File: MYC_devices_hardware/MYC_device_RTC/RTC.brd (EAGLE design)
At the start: 64.8 x 54.9 mm, 30 parts, among them IC1 MEGA8-P, IC2 7805T, Q1 20MHz, X1 8-15V, X2 1503_09, X3 1503_09

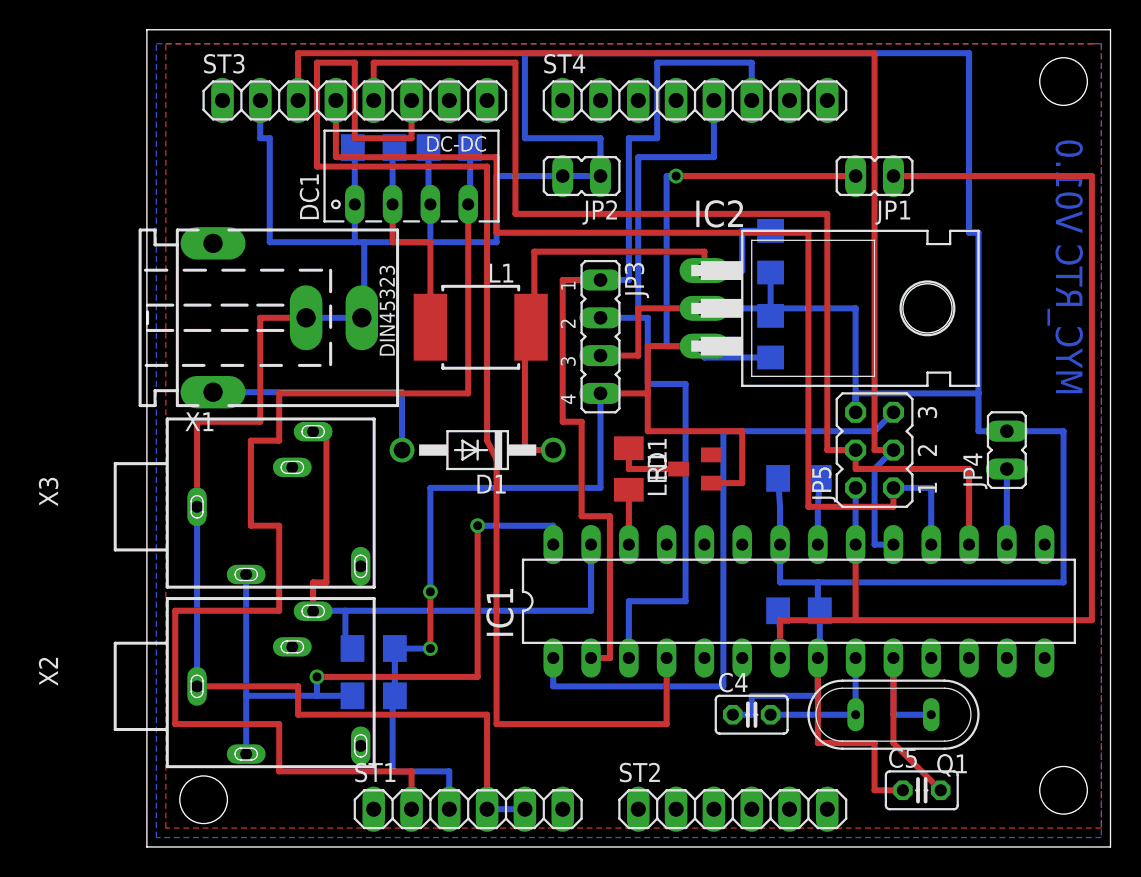
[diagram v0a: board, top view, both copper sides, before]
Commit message: some changes of DTMF devices
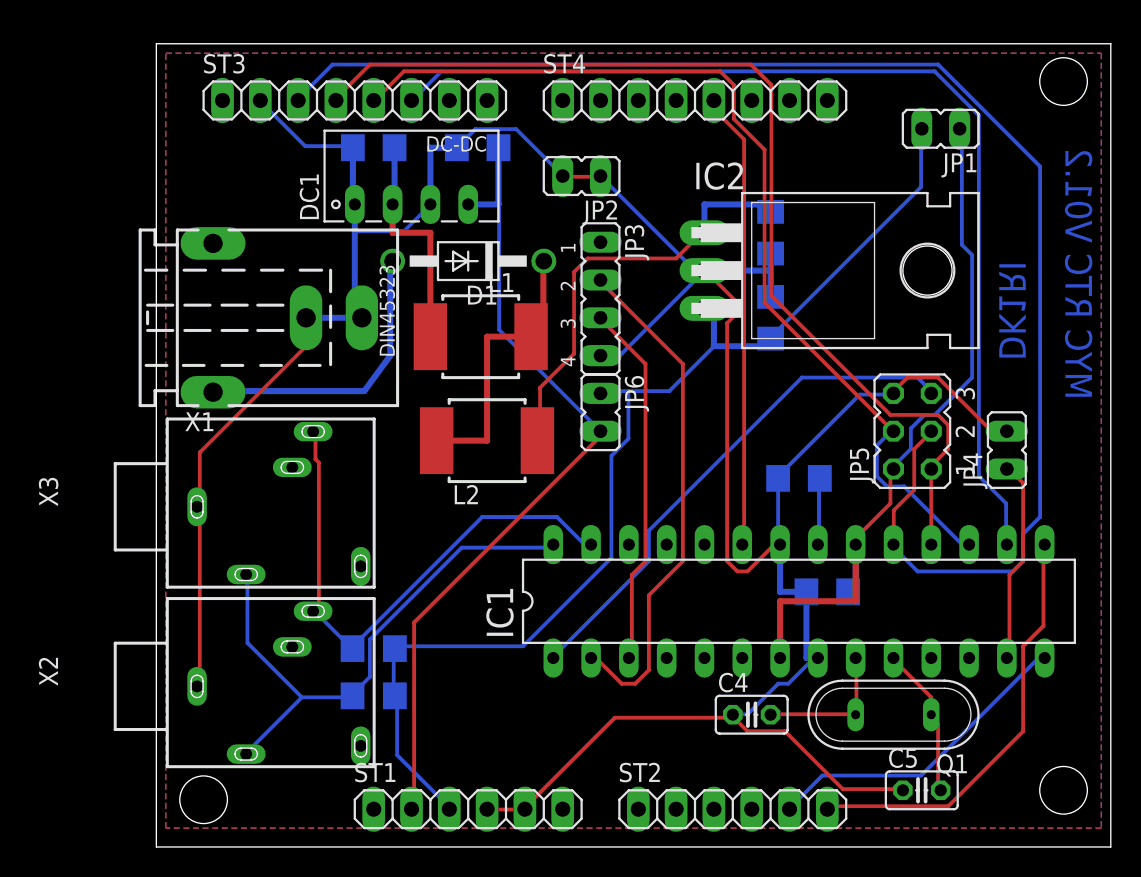
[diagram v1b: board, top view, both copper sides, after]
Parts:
- removed LED1: PL006-WCY01, led:SOT23
- removed R1: 4k7, resistor:M1206
- added JP6: USB2, jumper:JP1
- added L2: 100u, inductor-neosid:MS85
- moved D1 12.7 mm to (20.3, 39.4)
- moved JP1 5.46 mm to (52.1, 48.3)
- moved JP5 2.84 mm to (50.2, 27.9)
- moved IC2 2.54 mm to (46.4, 38.7)
- moved JP3 2.54 mm to (29.2, 36.8)
- moved C6 2.29 mm to (44.5, 17.1), turned to 0 degrees
- moved C7 1.90 mm to (21.0, 47.0)
- moved C2 1.27 mm to (40.6, 35.6)
- moved C1 1.27 mm to (40.6, 41.3)
- moved L1 0.63 mm to (21.2, 34.3)
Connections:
- removed net N$12: IC1.3, JP3.2, ST4.5
- removed net N$50: LED1.3, R1.1
- new net N$10: IC1.15, ST2.6
- new net N$7: D1.C, L1.1, L2.1
- new net N$8: IC1.3, JP3.3
- new net N$9: IC1.2, JP3.2
- net GND: now also JP3.4; no longer JP3.3
- net N$1: now also IC1.23, ST4.5; no longer IC1.26, R1.2
- net N$2: now also IC1.14, ST2.5; no longer IC1.2, JP3.1, ST4.6
- net N$33: now also L2.2; no longer D1.C, L1.1
- net N$4: now also IC1.16; no longer IC1.4
- net N$6: now also IC1.13; no longer IC1.16
- net VDD: now also JP6.1; no longer JP3.4, LED1.1
- net VSS: now also JP6.2
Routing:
- net GND: track 302.8 -> 200.9 mm
- net N$12: track 52.1 -> 0.00 mm
- net N$2: track 59.7 -> 21.4 mm
- net N$9: track 0.00 -> 34.5 mm
- net N$44: track 78.7 -> 48.5 mm
- net VSS: track 84.0 -> 54.7 mm
- net N$10: track 0.00 -> 28.5 mm
- net N$1: track 3.68 -> 30.8 mm
- net VDD: track 102.2 -> 75.9 mm, vias 3 -> 0
- net N$8: track 0.00 -> 24.6 mm
- net N$20: track 78.0 -> 99.3 mm
- net N$7: track 0.00 -> 18.8 mm
- net N$4: track 85.9 -> 69.8 mm
- net N$28: track 74.9 -> 64.8 mm
- net N$22: track 47.8 -> 37.8 mm, vias 2 -> 0
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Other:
- board size 64.8 x 54.9 mm -> 64.1 x 54 mm
- board text added: "DK1RI"
- board text added: "MYC RTC V01.2"
- board text removed: "MYC_RTC V01.0"
